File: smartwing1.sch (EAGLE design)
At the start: 61 parts, among them IC3 PIC24FJ64GB002, SW1 CT10-XXXX-A2, U1 SEN0142, U2 SN74LVC1T45DBVT, U3 SN74LVC1T45DBVT, U4 SN74LVC1T45DBVT, U5 SN74LVC1T45DBVT, U6 SN74LVC1T45DBVT, U7 SN74LVC1T45DBVT, U8 SN74LVC1T45DBVT

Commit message: taktak
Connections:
- net PIN8 renamed N$1
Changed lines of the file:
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@@
 <?xml version="1.0" encoding="utf-8"?>
 <!DOCTYPE eagle SYSTEM "eagle.dtd">
-<eagle version="9.6.2">
+<eagle version="9.6.1">
 <drawing>
 <settings>
@@
 </segment>
 </net>
-<net name="PIN8" class="0">
-<segment>
-<pinref part="IC3" gate="G$1" pin="TDI/RP7/PMD5/INT0/CN23/RB7"/>
-<wire x1="850.9" y1="-10.16" x2="863.6" y2="-10.16" width="0.1524" layer="91"/>
-<label x="858.52" y="-10.16" size="1.778" layer="95"/>
-</segment>
-</net>
 <net name="SDA" class="0">
 <segment>
@@
 </segment>
 </net>
+<net name="N$1" class="0">
+<segment>
+<pinref part="IC3" gate="G$1" pin="TDI/RP7/PMD5/INT0/CN23/RB7"/>
+<wire x1="850.9" y1="-10.16" x2="863.6" y2="-10.16" width="0.1524" layer="91"/>
+</segment>
+</net>

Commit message: tata
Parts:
- C4: value (none) -> 100nF
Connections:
- new net 100NF: C6.2, C7.1, IC2.GND
- new net N$17: C4.2, IC3.VDD@1
- net N$6: no longer C6.2, C7.1, IC2.GND
- net VCC: no longer C4.2, IC3.VDD@1
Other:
- note added: "100nF"

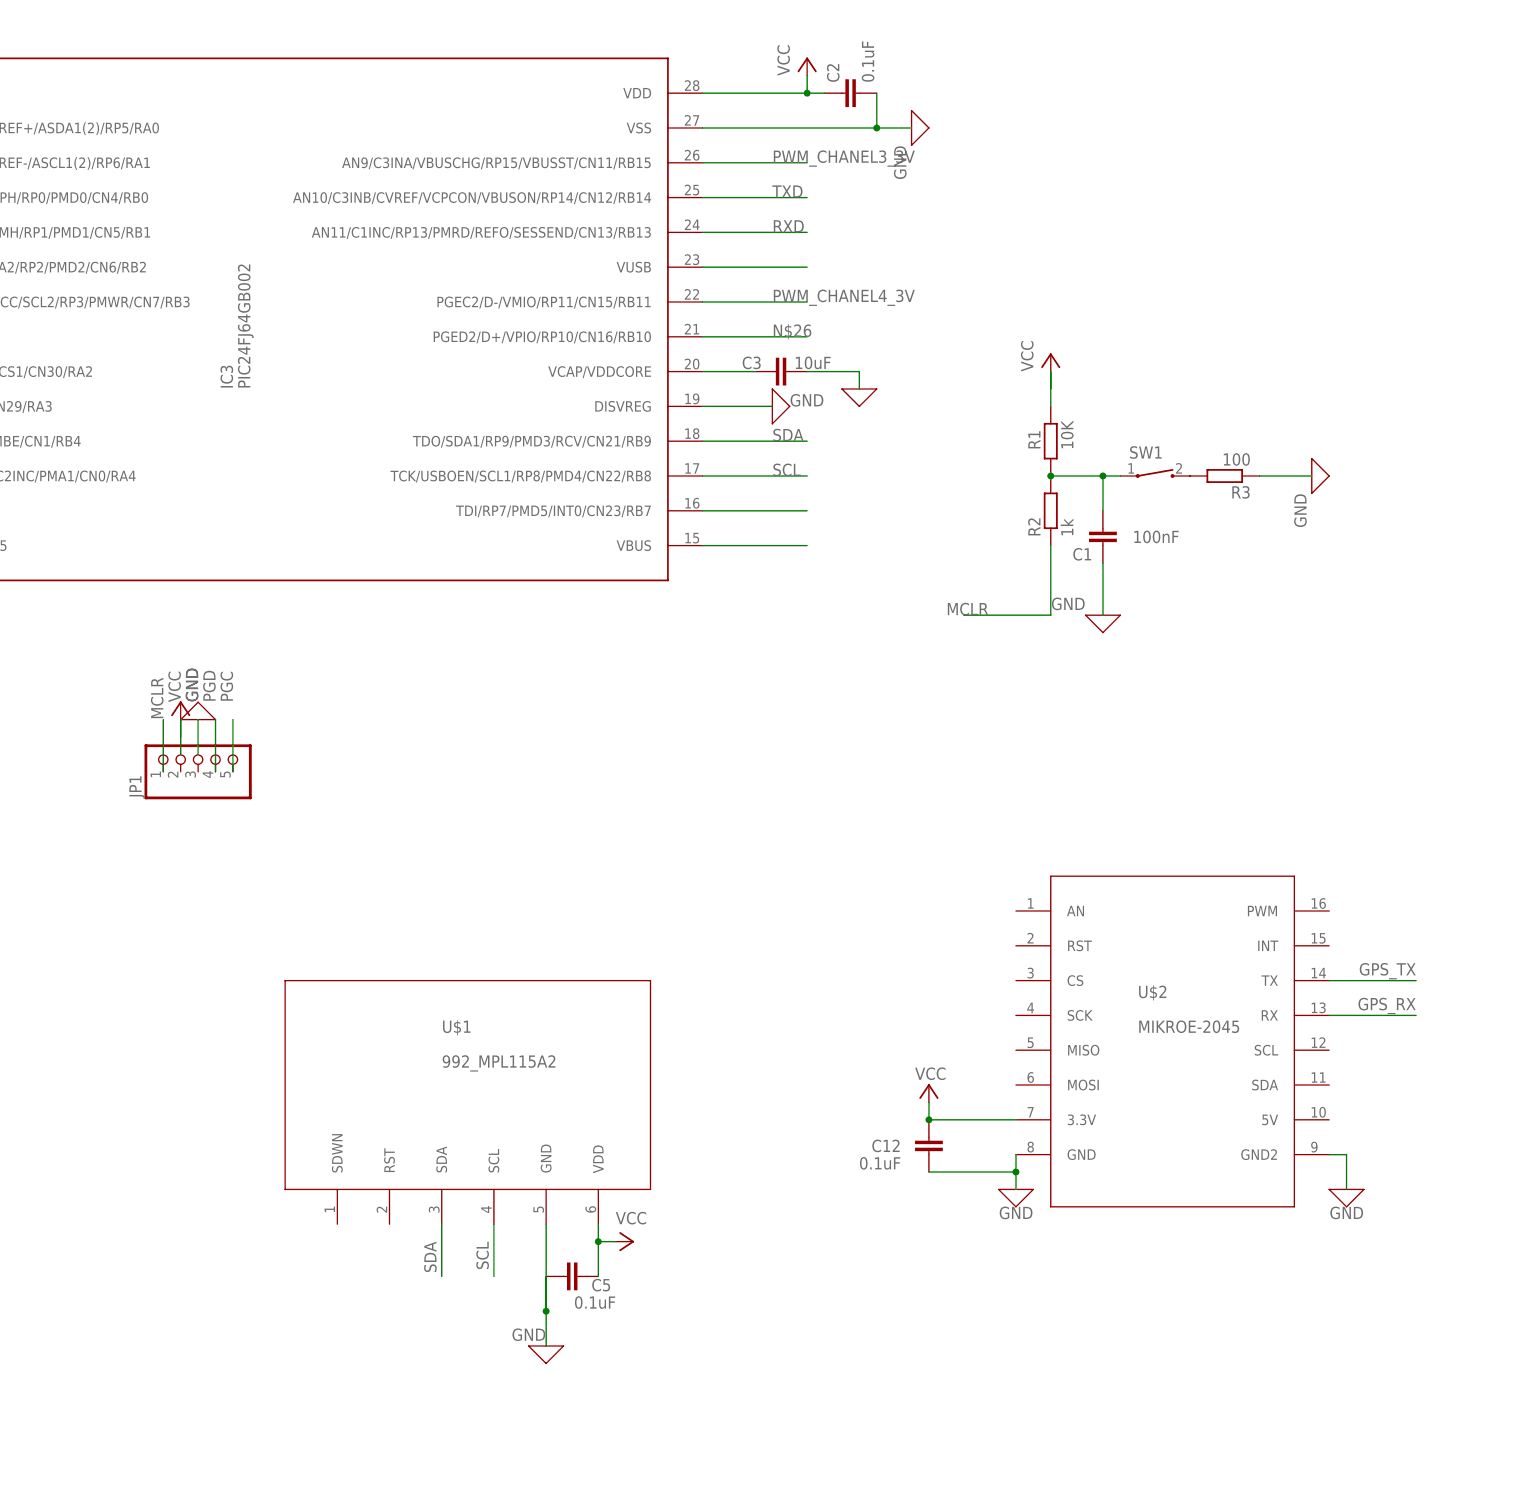
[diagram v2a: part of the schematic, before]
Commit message: Add FTDI
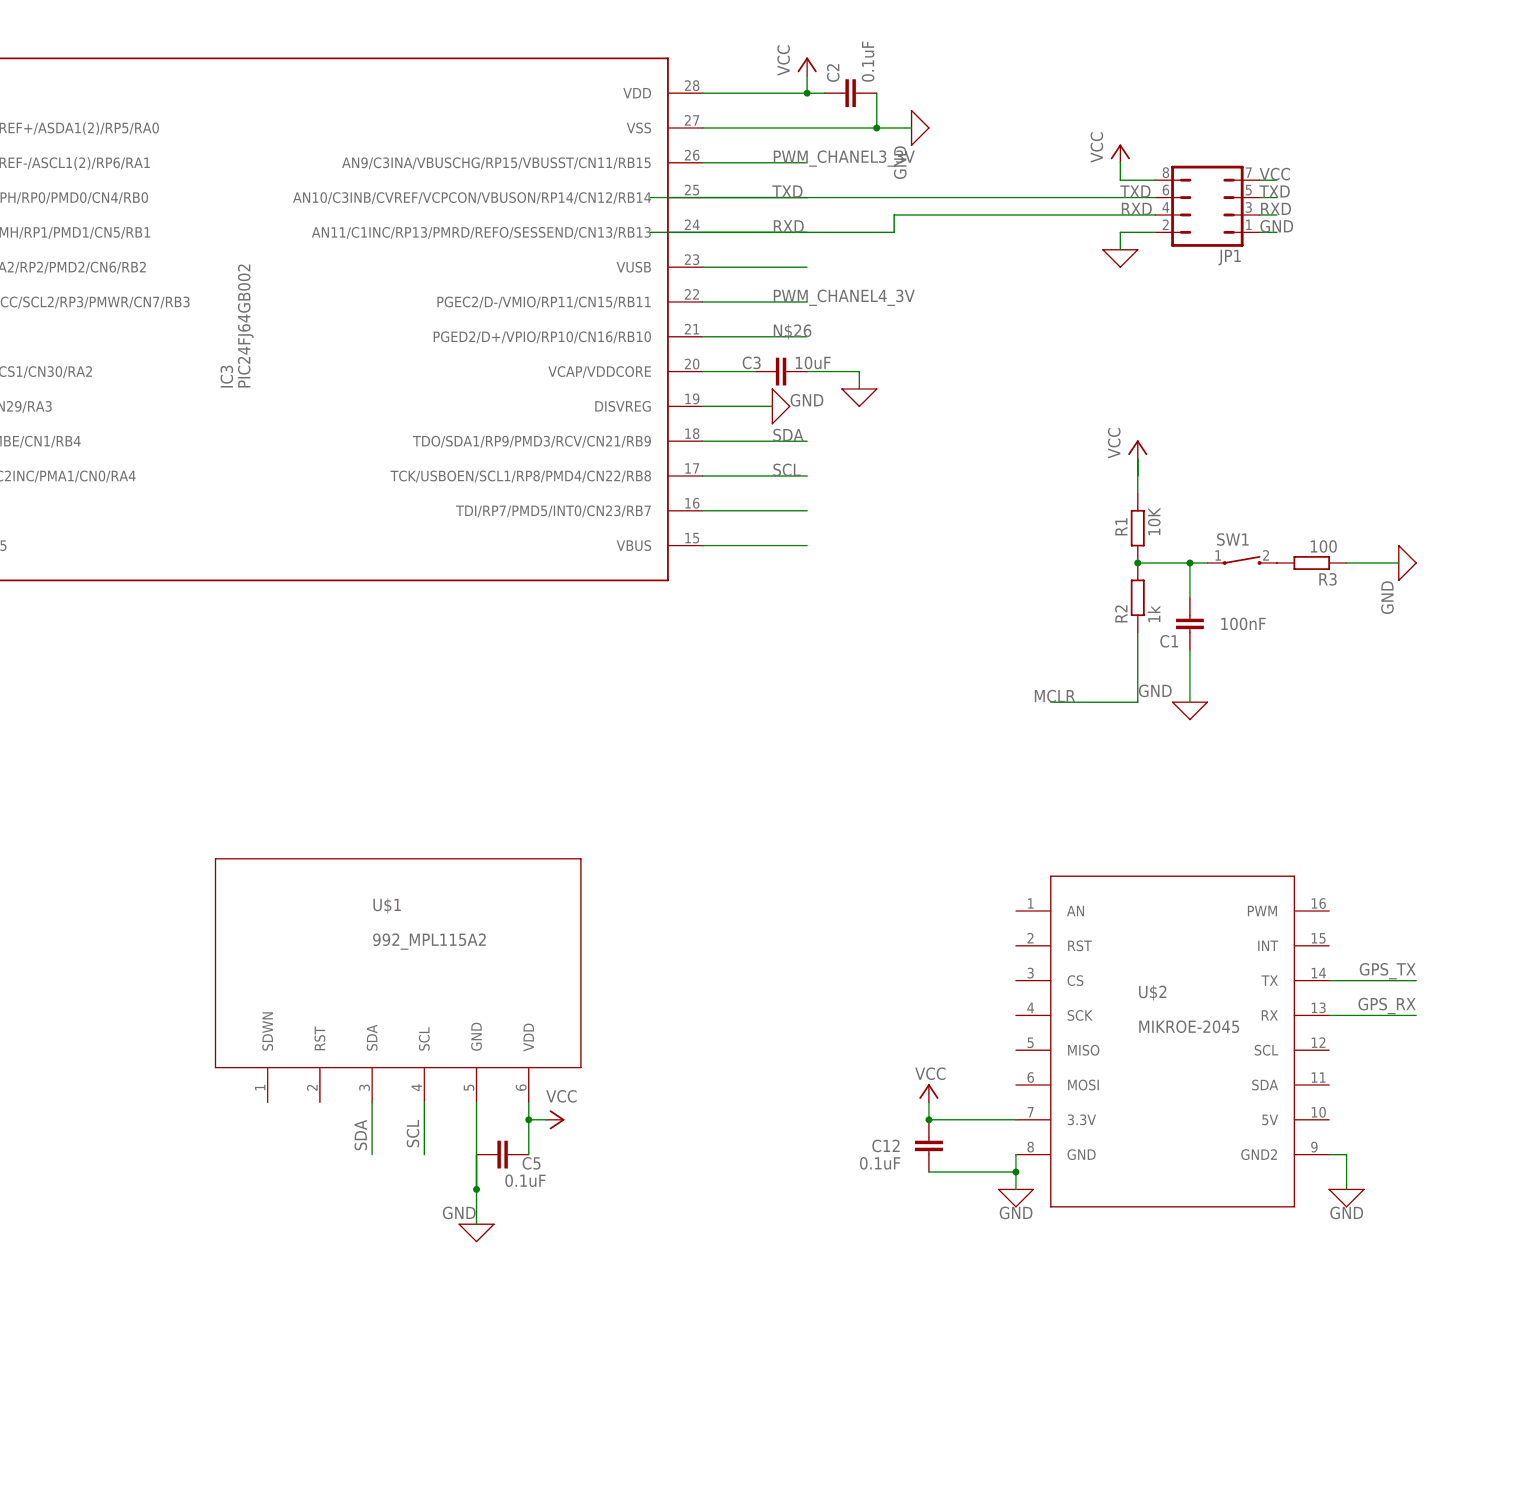
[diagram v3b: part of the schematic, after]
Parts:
- JP1: device pinhead:PINHD-1X5 -> jumper:JP4Q
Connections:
- net 0: now also JP1.2
- net GND: now also JP1.1
- net MCLR: no longer JP1.1
- net PGC: no longer JP1.5
- net PGD: no longer JP1.4
- net RXD: now also JP1.3, JP1.4
- net TXD: now also JP1.5, JP1.6
- net VCC: now also JP1.7, JP1.8
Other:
- moved on the sheet: C1, C5, R1, R2, R3, SW1, U$1

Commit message: finav
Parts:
- removed C22, C23, C24, C25, C26, C27, C28, C29: 100nF, rcl:C-EU075-032X103
- removed U2, U5, U6, U7: SN74LVC1T45DBVT, NEWCUSTOM:SN74LVC1T45DBVT
- added JP2: (no value), pinhead:PINHD-1X5
- added R13, R14: 20K, rcl:R-EU_0204/5
- added R4, R5: 10K, rcl:R-EU_0204/5
- IC1: value (none) -> Ubec
- IC2: value (none) -> MCP1702-3302E/T0
- R10, R9: value 4.7k -> 10K; device rcl:R-EU_0207/7 -> rcl:R-EU_0204/5
- R11, R12: value 4.7k -> 20K; device rcl:R-EU_0207/7 -> rcl:R-EU_0204/5
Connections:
- removed net N$10: R9.2, U2.DIR
- removed net N$12: C14.1, U1.VIN
- removed net N$14: R10.2, U5.DIR
- removed net N$15: R11.2, U6.DIR
- removed net N$16: R12.2, U7.DIR
- removed net PIN4: CHANEL1.3
- removed net PIN5: CHANEL2.3
- removed net PIN6: CHANEL3.3
- removed net PIN7: CHANEL4.3
- net 0: now also R13.1, R14.1; no longer C23.2, C25.2, C27.2, C29.2, R10.1, R9.1
- net GND: now also JP2.3
- net MCLR: now also JP2.5
- net N$13: no longer C23.1, C25.1, C27.1, C29.1, U2.VCCB, U5.VCCB, U6.VCCB, U7.VCCB
- net N$3: no longer C22.1, C24.1, C26.1, C28.1, U2.VCCA, U5.VCCA, U6.VCCA, U7.VCCA
- net N$6: no longer C22.2, C24.2, C26.2, C28.2, U2.GND, U5.GND, U6.GND, U7.GND
- net PGC: now also JP2.1
- net PGD: now also JP2.2
- net PWM_CHANEL1_3V: now also IC3.AN4/C1INB/DPLN/SDA2/RP2/PMD2/CN6/RB2, R11.2, R4.2; no longer U2.A
- net PWM_CHANEL1_5V: now also CHANEL1.3, R4.1; no longer U2.B
- net PWM_CHANEL2_3V: now also IC3.AN5/C1INA/DMLN/RTCC/SCL2/RP3/PMWR/CN7/RB3, R12.2, R5.2; no longer U5.A
- net PWM_CHANEL2_5V: now also CHANEL2.3, R5.1; no longer U5.B
- net PWM_CHANEL3_3V: now also R13.2, R9.2; no longer U6.A
- net PWM_CHANEL3_5V: now also CHANEL3.3, R9.1; no longer U6.B
- net PWM_CHANEL4_3V: now also R10.2, R14.2; no longer U7.A
- net PWM_CHANEL4_5V: now also CHANEL4.3, R10.1; no longer U7.B
- net VBAT: no longer C6.1, IC2.IN
- net VCC: now also C14.1, JP2.4, U1.VIN
- net VCC1: now also C6.1, IC2.IN
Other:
- note added: "ALIM"
- note added: "ALIM1"
- note added: "BRUSHLESS"
- note added: "FTDI1"
- note added: "GPS"
- note added: "MPL115"
- note added: "REHAUSSEUR_DE_TENSION_3V3_VERS_5V"
- note added: "REST"
- note added: "RX"
- note added: "SEN0142"
- note added: "SERVO"
- moved on the sheet: C11, CHANEL1, CHANEL2, CHANEL3, CHANEL4, R10, R11, R12, R9

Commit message: prog
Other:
- note added: "PROG"
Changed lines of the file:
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@@
 <text x="800.1" y="-50.8" size="1.778" layer="91">MPL115</text>
 <text x="683.26" y="-58.42" size="1.778" layer="91">SEN0142</text>
+<text x="751.84" y="-25.4" size="1.778" layer="91">PROG</text>
 </plain>
 <instances>
